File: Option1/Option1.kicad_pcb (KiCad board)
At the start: 2 copper layers, 85 x 76.5 mm, 120 parts, among them J1401 10118194-0001LF, J1402 Conn_01x06_Pin, J1501 GH-13AB, J1801 Conn_01x08_Socket, J401 Conn_01x05_Pin, J402 Conn_01x04_Pin, J403 Conn_01x05_Pin, J503 KF2EDGKRG-3.5-2*7P, J999 Phoenix_Connetor_07x2pin_toWi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, Q1001 JY2302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

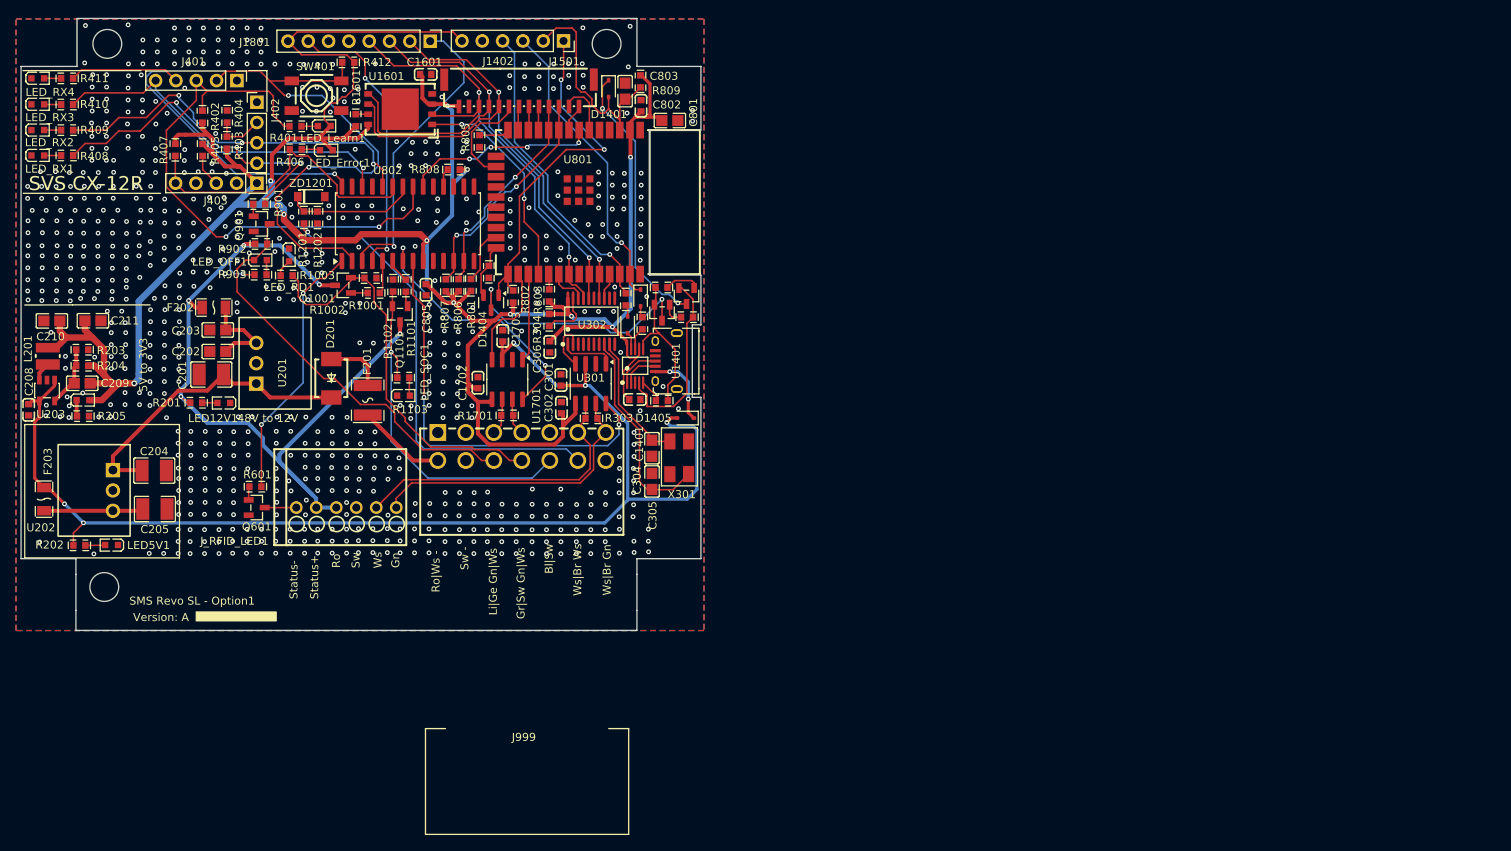
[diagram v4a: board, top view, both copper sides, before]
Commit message: Layout komplett neu überarbeitet, Neu Pinbelegung MCT, USB beschaltung muss noch korrigert werden
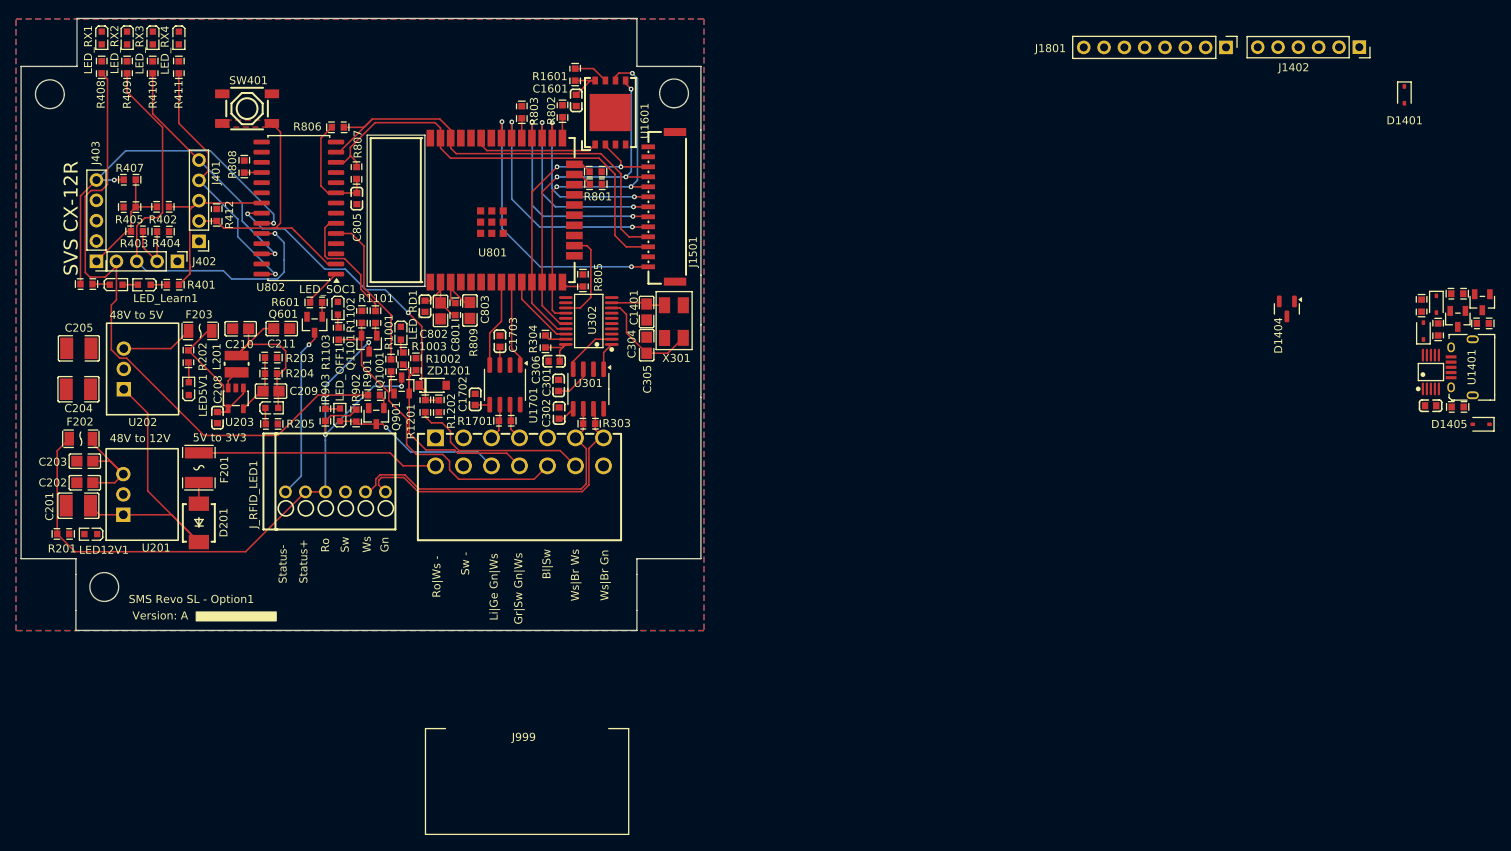
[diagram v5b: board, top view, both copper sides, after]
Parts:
- moved D1405 99.5 mm to (283.5, 94.7)
- moved Q1401 99.5 mm to (283.6, 79.4)
- moved R1402 99.5 mm to (280.5, 78.4)
- moved R1403 99.5 mm to (280.5, 92.5)
- moved U1401 99.5 mm to (277.2, 88.2)
- moved D1401 99.5 mm to (273.9, 53.5)
- moved D1402 99.5 mm to (276.3, 83.0)
- moved D1403 99.5 mm to (277.9, 79.7)
- moved D1404 99.5 mm to (259.2, 80.3)
- moved J1401 99.5 mm to (281.1, 87.6)
- moved J1402 99.5 mm to (268.2, 47.6)
- moved J1801 99.5 mm to (251.6, 47.6)
- moved Q1402 99.5 mm to (280.6, 81.5)
- moved R1404 99.5 mm to (283.7, 82.1)
- moved C1401 99.5 mm to (277.2, 92.4)
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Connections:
- D1403 pad 1: IO23 -> IO3
- J1402 pad 3: IO23 -> IO3
- J1402 pad 4: IO22 -> IO1
- J1501 pad 1: IO32 -> IO19
- J1501 pad 10: IO21 -> IO27
- J1501 pad 11: IO19 -> IO26
- J1501 pad 3: IO33 -> IO23
- J1501 pad 4: IO25 -> IO22
- J1501 pad 5: IO26 -> IO18
- J1501 pad 6: IO27 -> IO17
- J1501 pad 7: IO14 -> IO16
- J1501 pad 8: IO13 -> IO4
- J1501 pad 9: IO3 -> IO14
- J1801 pad 2: IO3 -> IO14
- J1801 pad 3: IO21 -> IO27
- J1801 pad 4: IO19 -> IO26
- R1401 pad 2: IO22 -> IO1
- R806 pad 1: IO25 -> IO22
- R807 pad 1: IO33 -> IO23
- U1601 pad 1: IO17 -> IO21
- U1601 pad 2: IO19 -> IO26
- U1601 pad 5: IO21 -> IO27
- U1601 pad 6: IO3 -> IO14
- U1701 pad 1: IO16 -> IO33
- U1701 pad 4: IO4 -> IO32
- U302 pad 13: IO1 -> IO13
- U302 pad 14: IO3 -> IO14
- U302 pad 16: IO21 -> IO27
- U302 pad 17: IO19 -> IO26
- U302 pad 18: IO18 -> IO25
- U802 pad 12: IO33 -> IO23
- U802 pad 13: IO25 -> IO22
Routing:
- net 3.3V: track 365.6 -> 80.1 mm, vias 11 -> 0
- net 5V: track 157.0 -> 25.2 mm, vias 5 -> 0
- net IO3: track 68.4 -> 0.00 mm, vias 2 -> 0
- net IO21: track 69.2 -> 15.7 mm, vias 2 -> 0
- net /CAN2_Tranciever/CAN_S-Mode: track 52.7 -> 0.00 mm, vias 2 -> 0
- net LED_Modus: track 70.6 -> 24.7 mm, vias 2 -> 0
- net IO14: track 3.00 -> 46.5 mm, vias 0 -> 3
- net IO0: track 44.7 -> 2.61 mm, vias 2 -> 0
- net IO27: track 2.99 -> 44.8 mm, vias 0 -> 3
- net RX_1: track 41.9 -> 82.3 mm, vias 3 -> 0
- net /MCT  Wlan/SPI_CS_RFID: track 37.7 -> 0.00 mm, vias 1 -> 0
- net IO26: track 2.98 -> 38.9 mm, vias 0 -> 2
- net /MCT  Wlan/SPI_RST_RFID: track 35.9 -> 0.00 mm, vias 2 -> 0
- net /Stecker Input/VCU_LED: track 57.9 -> 22.7 mm, vias 1 -> 0
- net Lernmodus: track 67.8 -> 33.5 mm, vias 2 -> 0
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- added copper zone on F.Cu, net Lernmodus
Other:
- outline, holes or cut-outs redrawn
- board text added: "48V to 5V"

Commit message: Kleine Änderungen
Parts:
- removed C1401: 100nF, easyeda2kicad:C0603
- removed D1401, D1402, D1403, D1405: 1N5819WS, Diode_SMD:D_SOD-323
- removed D1404: BAT54C, Package_TO_SOT_SMD:SOT-23
- removed J1401: 10118194-0001LF, easyeda2kicad:MICRO-USB-SMD_10118194-0001LF
- removed J1402: Conn_01x06_Pin, Connector_PinSocket_2.54mm:PinSocket_1x06_P2.54mm_Vertical
- removed Q1401, Q1402: BC817-40, easyeda2kicad:SOT-23-3_L2.9-W1.3-P1.90-LS2.4-BR
- removed R1401, R1405: 500Ω, easyeda2kicad:R0603
- removed R1402, R1404: 2k2, easyeda2kicad:R0603
- removed R1403: 4k7, easyeda2kicad:R0603
- removed U1401: CH340X, easyeda2kicad:MSOP-10_L3.0-W3.0-P0.50-LS5.0-BL
- moved C201 0.32 mm to (108.4, 104.9)
- moved ZD1201 0.21 mm to (152.6, 89.8)
- moved R801 0.18 mm to (173.0, 64.7)
- moved R804 0.14 mm to (172.9, 63.1)
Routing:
- net 3.3V: track 80.1 -> 354.3 mm, vias 0 -> 11
- net 5V: track 25.2 -> 108.8 mm, vias 0 -> 2
- net /CAN2_Tranciever/CAN_S-Mode: track 0.00 -> 50.7 mm, vias 0 -> 2
- net IO35: track 0.00 -> 45.8 mm, vias 0 -> 2
- net /CAN1 Tranciever/CAN_S-Mode: track 0.00 -> 38.1 mm, vias 0 -> 2
- net IO34: track 0.00 -> 22.9 mm, vias 0 -> 2
- net Lernmodus: track 33.5 -> 42.6 mm, vias 0 -> 2
- net Net-(U202-Vout): track 9.02 -> 13.1 mm
- net TX_Analog: track 0.00 -> 4.10 mm
- net 48V_Fused: track 38.4 -> 42.2 mm
- net 12V: track 91.4 -> 88.5 mm, vias 3 -> 4
- net /MCT  Wlan/TX_3 (SOC): track 15.9 -> 18.3 mm
- net IO19: track 35.7 -> 33.4 mm
- net Net-(LED_RX3-A): track 0.00 -> 2.13 mm
- net Net-(LED_RX4-A): track 0.00 -> 2.12 mm
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- removed copper zone on F.Cu, net Lernmodus
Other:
- board size 85 x 76.5 mm -> 85 x 67.5 mm
- board text removed: "USB"

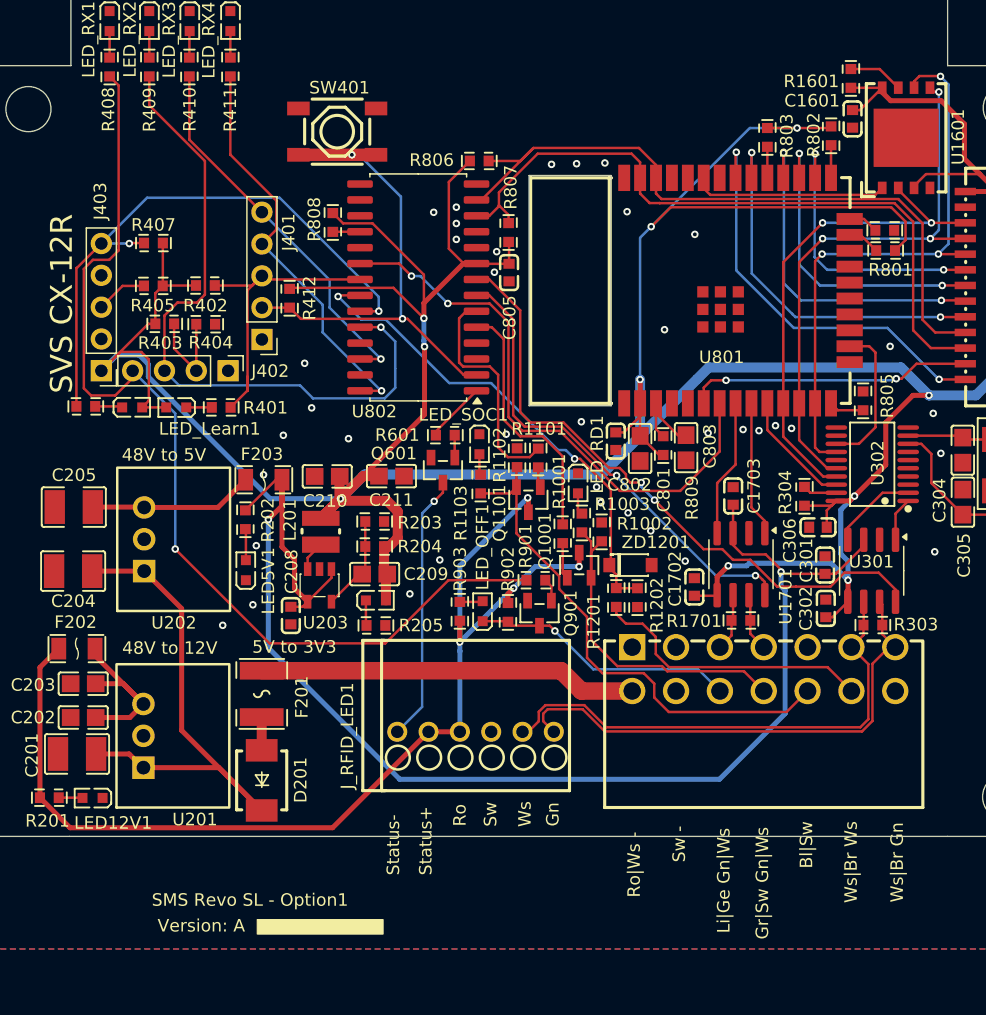
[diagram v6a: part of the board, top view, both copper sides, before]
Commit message: power Supply angepasst für 12V und 48V, Datenblätter für DCDCs hinzugefügt
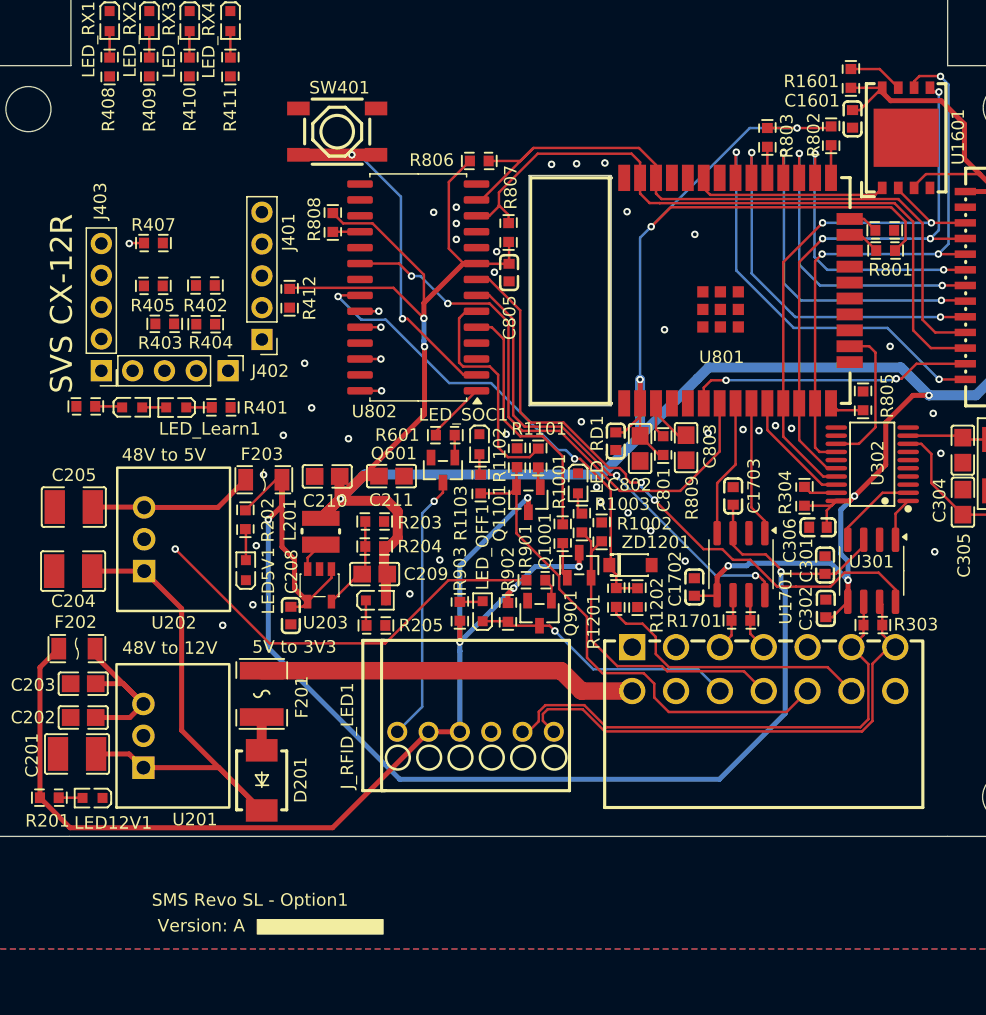
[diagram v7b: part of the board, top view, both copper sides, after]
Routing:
- net RX_2: track 54.3 -> 1.67 mm
- net 3.3V: track 354.3 -> 305.4 mm
- net RX_1: track 81.3 -> 33.2 mm
- net Fehler_LED: track 46.9 -> 2.70 mm
- net RX_4: track 32.8 -> 1.75 mm
- net RX_3: track 30.6 -> 1.68 mm
- net LED_Modus: track 24.7 -> 0.00 mm
- net Lernmodus: track 42.6 -> 31.0 mm
- net F2_Sel: track 8.24 -> 0.00 mm
- net TX_Analog: track 4.10 -> 0.00 mm
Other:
- board text added: "1"
- board text added: "13"
- board text added: "14"
- board text added: "2"
- board text added: "48V_IN (2)"
- board text added: "CAN2_H (13)"
- board text added: "bl/sw"
- board text added: "gn"
- board text added: "gn/ws"
- board text added: "gr/sw"
- board text added: "li/ge"
- board text added: "oben"
- board text added: "ro"
- board text added: "ro/ws"
- board text added: "sw"
- board text added: "unten"
- board text added: "ws"
- board text added: "ws/br"
- board text added: "ws/gn"
- board text added: "x"
- board text removed: "48V_IN"
- board text removed: "Bl|Sw"
- board text removed: "CAN2_H"
- board text removed: "Gn"
- board text removed: "Gr|Sw Gn|Ws"
- board text removed: "Li|Ge Gn|Ws"
- board text removed: "Ro"
- board text removed: "Ro|Ws -"
- board text removed: "Sw"
- board text removed: "Sw -"
- board text removed: "Ws"
- board text removed: "Ws|Br Gn"
- board text removed: "Ws|Br Ws"
